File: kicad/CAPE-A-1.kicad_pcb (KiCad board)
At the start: 4 copper layers, 55 x 35 mm, 31 parts

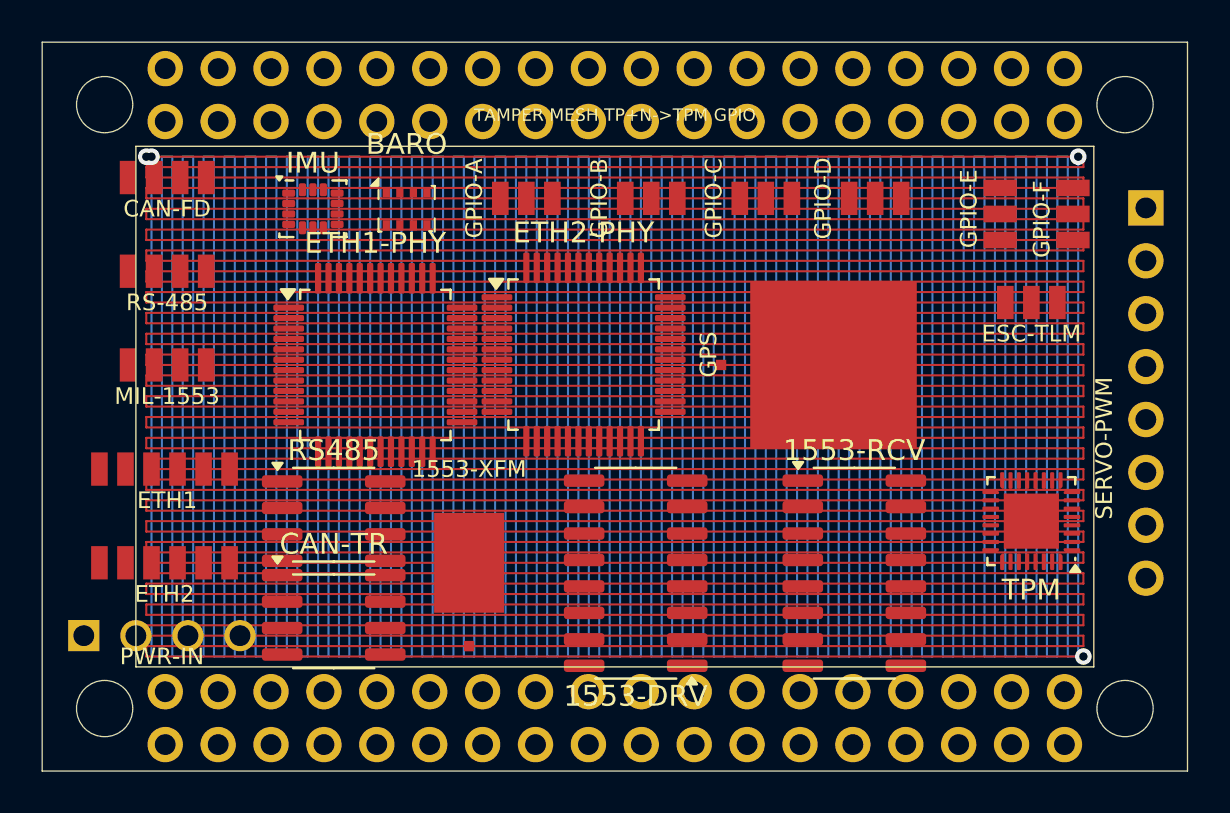
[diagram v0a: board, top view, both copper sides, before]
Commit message: updated the xcvr to fix drc issues an
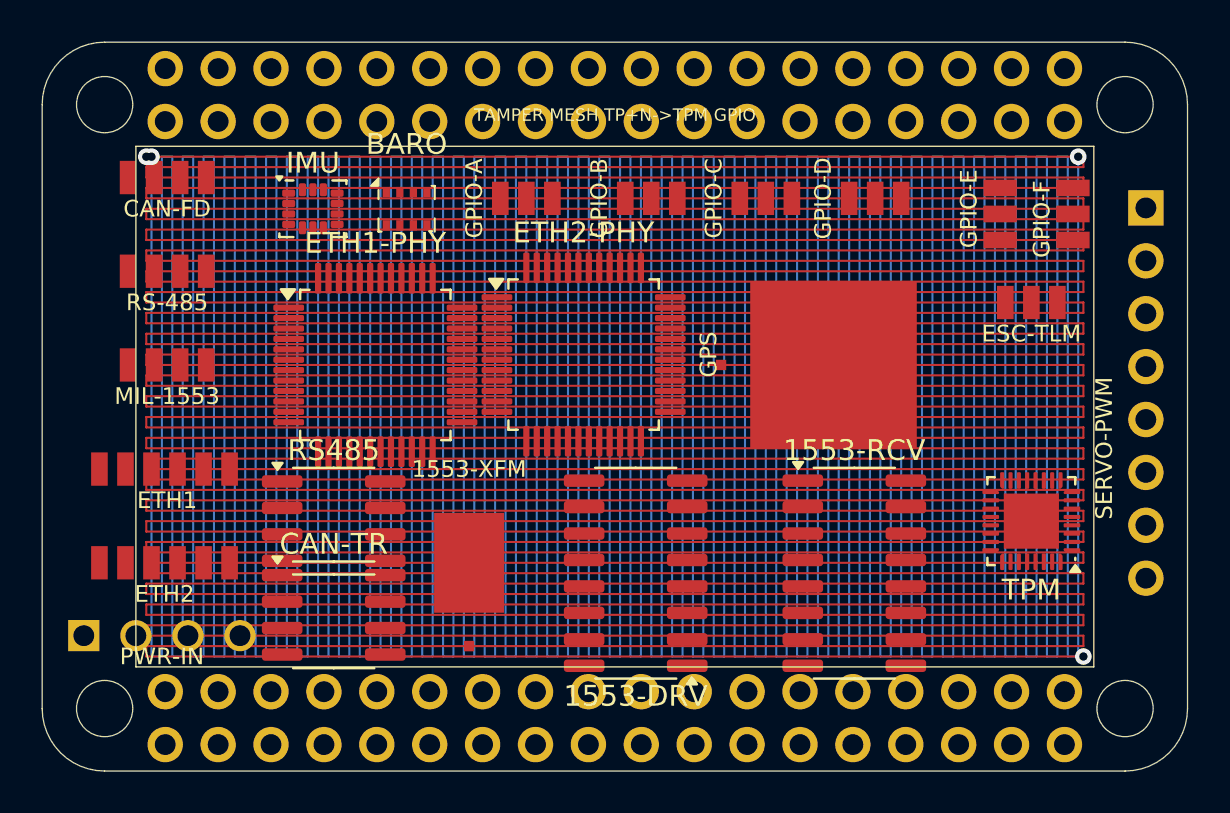
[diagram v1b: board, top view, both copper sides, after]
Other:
- outline, holes or cut-outs redrawn
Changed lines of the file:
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@@
 		(embedded_fonts no)
 	)
-	(gr_line
-		(start 121 87.5)
-		(end 176 87.5)
+	(gr_arc
+		(start 121 90.5)
+		(mid 121.87868 88.37868)
+		(end 124 87.5)
 		(stroke
 			(width 0.05)
@@
 	)
 	(gr_line
-		(start 176 122.5)
-		(end 121 122.5)
+		(start 124 87.5)
+		(end 173 87.5)
+		(stroke
+			(width 0.05)
+			(type solid)
+		)
+		(layer "Edge.Cuts")
+	)
+	(gr_arc
+		(start 173 87.5)
+		(mid 175.12132 88.37868)
+		(end 176 90.5)
 		(stroke
 			(width 0.05)
@@
 	)
 	(gr_line
-		(start 121 122.5)
-		(end 121 87.5)
+		(start 176 90.5)
+		(end 176 119.5)
+		(stroke
+			(width 0.05)
+			(type solid)
+		)
+		(layer "Edge.Cuts")
+	)
+	(gr_arc
+		(start 176 119.5)
+		(mid 175.12132 121.62132)
+		(end 173 122.5)
 		(stroke
 			(width 0.05)
@@
 	)
 	(gr_line
-		(start 176 87.5)
-		(end 176 122.5)
+		(start 173 122.5)
+		(end 124 122.5)
 		(stroke
 			(width 0.05)
+			(type solid)
+		)
+		(layer "Edge.Cuts")
+	)
+	(gr_arc
+		(start 124 122.5)
+		(mid 121.87868 121.62132)
+		(end 121 119.5)
+		(stroke
+			(width 0.05)
+			(type solid)
+		)
+		(layer "Edge.Cuts")
+	)
+	(gr_line
+		(start 121 119.5)
+		(end 121 90.5)
+		(stroke
+			(width 0.05)
